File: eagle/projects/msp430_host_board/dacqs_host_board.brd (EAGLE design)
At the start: 127 x 100 mm, 272 parts, among them J1 MOL-SL-4-RA, J10 MOL-SL-3-V, J11 MOL-SL-2-V, J12 CONN HEADER 20POS .100" DBL, J13 MOL-SL-2-RA, J14 USB_MICROB_RECPT, J16 MOL-SL-2-RA, J17 CLM-112-02-L-D-IMU-MOUNT_IMU, J18 MOLSL-7-RA, J19 CONN HEADER 20POS .100" DBL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

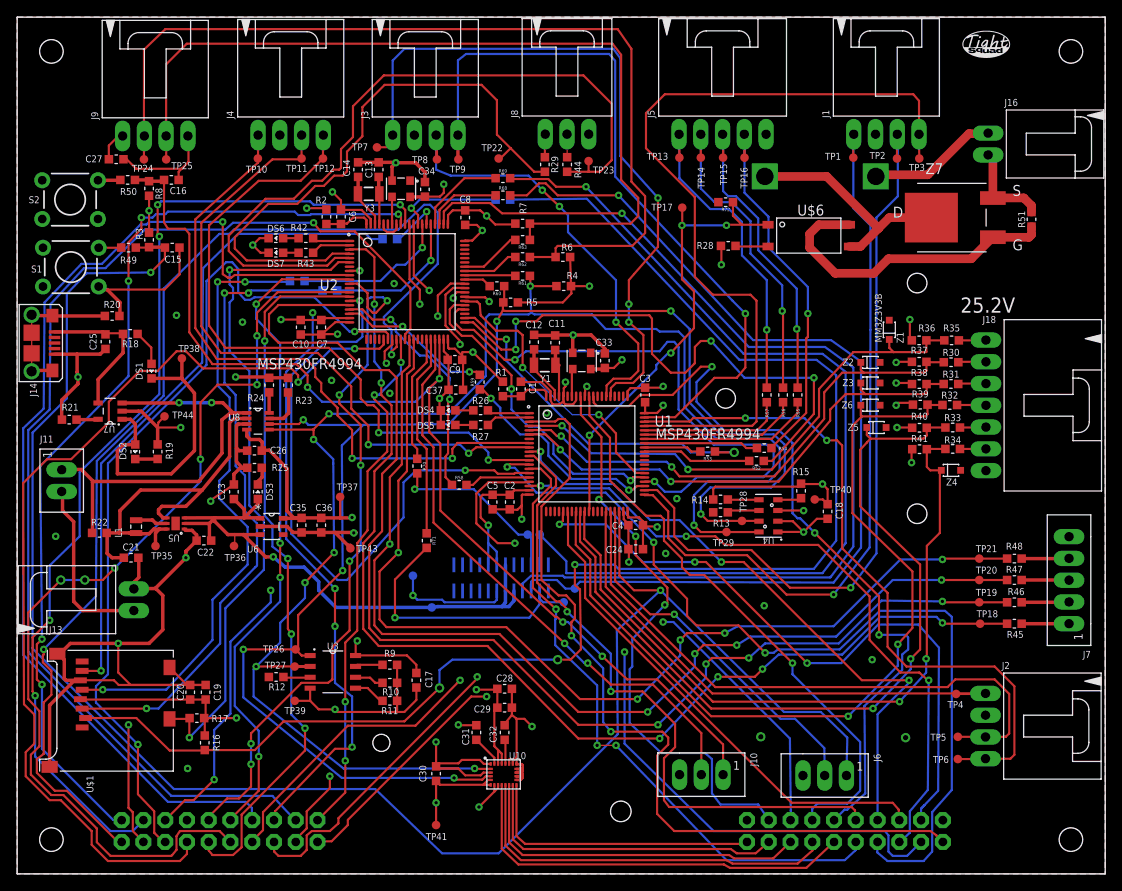
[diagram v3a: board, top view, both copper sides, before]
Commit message: Changed the power fet symbol and attached the powerpad on the 5V boost to ground pour
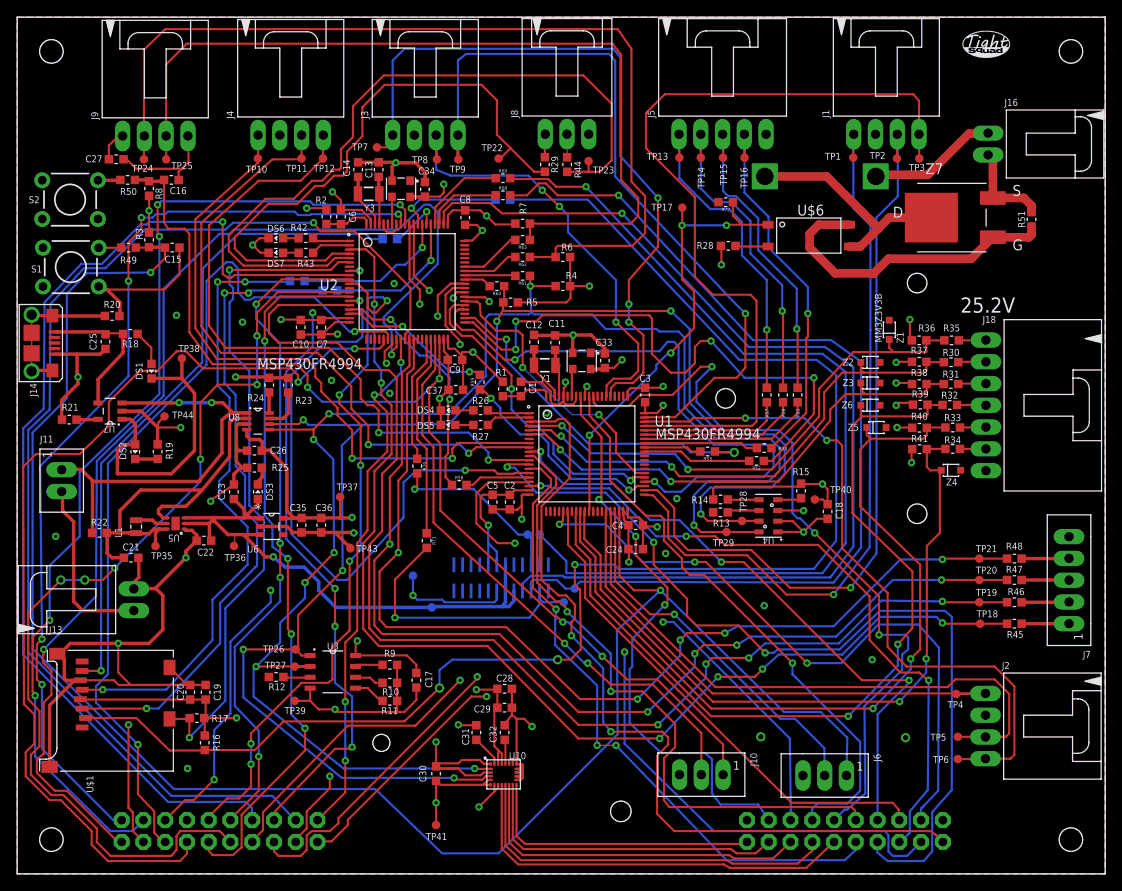
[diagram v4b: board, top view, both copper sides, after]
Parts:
- moved R4 0.10 mm to (63.7, 69.6)
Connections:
- removed net N$42: U5.7
- net GND: now also U5.7
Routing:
- net P7.2_2: track 115.0 -> 116.3 mm
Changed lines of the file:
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@@
 <layer number="14" name="Route14" color="1" fill="6" visible="no" active="no"/>
 <layer number="15" name="Route15" color="4" fill="6" visible="yes" active="yes"/>
-<layer number="16" name="Bottom" color="1" fill="1" visible="no" active="yes"/>
+<layer number="16" name="Bottom" color="1" fill="1" visible="yes" active="yes"/>
 <layer number="17" name="Pads" color="2" fill="1" visible="yes" active="yes"/>
 <layer number="18" name="Vias" color="2" fill="1" visible="yes" active="yes"/>
@@
 <attribute name="VALUE" value="1.02k" x="105.41" y="56.52" size="0.254" layer="27" ratio="6" rot="R180" align="center"/>
 </element>
-<element name="R4" library="daqcs_host" package="R0603" value="2.61k" x="63.8" y="69.6" smashed="yes">
-<attribute name="MANUFACTURER" value="Panasonic" x="63.8" y="69.6" size="1.778" layer="27" display="off"/>
-<attribute name="MANUFACTURER_PN" value="ERJ-3EKF2611V" x="63.8" y="69.6" size="1.778" layer="27" display="off"/>
-<attribute name="VENDOR" value="Digi-key" x="63.8" y="69.6" size="1.778" layer="27" display="off"/>
-<attribute name="POWER" value="1/10W" x="63.8" y="69.6" size="1.778" layer="27" display="off"/>
-<attribute name="VENDOR_PN" value="P2.61KHCT-ND" x="63.8" y="69.6" size="1.778" layer="27" display="off"/>
-<attribute name="TOLERANCE" value="1%" x="63.8" y="69.6" size="1.778" layer="27" display="off"/>
-<attribute name="NAME" x="64.8" y="70.85" size="0.8128" layer="25" ratio="15" align="center"/>
-<attribute name="VALUE" x="63.8" y="68.85" size="0.254" layer="27" ratio="6" align="center"/>
+<element name="R4" library="daqcs_host" package="R0603" value="2.61k" x="63.7" y="69.6" smashed="yes">
+<attribute name="MANUFACTURER" value="Panasonic" x="63.7" y="69.6" size="1.778" layer="27" display="off"/>
+<attribute name="MANUFACTURER_PN" value="ERJ-3EKF2611V" x="63.7" y="69.6" size="1.778" layer="27" display="off"/>
+<attribute name="VENDOR" value="Digi-key" x="63.7" y="69.6" size="1.778" layer="27" display="off"/>
+<attribute name="POWER" value="1/10W" x="63.7" y="69.6" size="1.778" layer="27" display="off"/>
+<attribute name="VENDOR_PN" value="P2.61KHCT-ND" x="63.7" y="69.6" size="1.778" layer="27" display="off"/>
+<attribute name="TOLERANCE" value="1%" x="63.7" y="69.6" size="1.778" layer="27" display="off"/>
+<attribute name="NAME" x="64.7" y="70.85" size="0.8128" layer="25" ratio="15" align="center"/>
+<attribute name="VALUE" x="63.7" y="68.85" size="0.254" layer="27" ratio="6" align="center"/>
 </element>
 <element name="R40" library="daqcs_host" package="R0603" value="4.32k" x="105.32" y="53.07" smashed="yes" rot="R180">
@@
 <wire x1="68.6" y1="60.05" x2="69.65" y2="60.05" width="0.254" layer="1"/>
 <wire x1="69.65" y1="60.05" x2="70.6" y2="61" width="0.254" layer="1"/>
-<wire x1="58.45" y1="67.7" x2="63.7" y2="67.7" width="0.254" layer="1"/>
-<wire x1="63.7" y1="67.7" x2="64.7" y2="68.75" width="0.254" layer="1"/>
-<wire x1="64.7" y1="68.75" x2="64.65" y2="69.6" width="0.254" layer="1"/>
+<wire x1="58.45" y1="67.7" x2="64.1" y2="67.7" width="0.254" layer="1"/>
 <wire x1="55.275" y1="13.835" x2="54.465" y2="13.835" width="0.254" layer="1"/>
 <wire x1="54.465" y1="13.835" x2="54" y2="14.3" width="0.254" layer="1"/>
@@
 <wire x1="49.15" y1="13.3" x2="48.9" y2="13.55" width="0.254" layer="1"/>
 <via x="66.8" y="69.6" extent="1-16" drill="0.381"/>
-<wire x1="66.8" y1="69.6" x2="64.65" y2="69.6" width="0.254" layer="1"/>
+<wire x1="66.8" y1="69.6" x2="64.55" y2="69.6" width="0.254" layer="1"/>
 <wire x1="35.55" y1="63.8" x2="35.5" y2="63.95" width="0.254" layer="1"/>
 <wire x1="37.15" y1="65.4" x2="35.5" y2="63.95" width="0.254" layer="1"/>
@@
 <wire x1="71.6" y1="57.7" x2="73.25" y2="57.7" width="0.254" layer="1"/>
 <wire x1="73.25" y1="57.7" x2="73.3" y2="57.75" width="0.254" layer="1"/>
-<wire x1="64.65" y1="69.6" x2="64.55" y2="73" width="0.254" layer="1"/>
+<wire x1="64.55" y1="69.6" x2="64.55" y2="73" width="0.254" layer="1"/>
 <wire x1="54.8" y1="77.8" x2="55.8" y2="76.8" width="0.254" layer="1"/>
 <wire x1="55.8" y1="76.8" x2="58.05" y2="76.8" width="0.254" layer="1"/>
 <wire x1="58.05" y1="76.8" x2="58.15" y2="76.9" width="0.254" layer="1"/>
+<wire x1="64.1" y1="67.7" x2="64.6" y2="68.2" width="0.254" layer="1"/>
+<wire x1="64.6" y1="68.2" x2="64.6" y2="69.55" width="0.254" layer="1"/>
+<wire x1="64.6" y1="69.55" x2="64.55" y2="69.6" width="0.254" layer="1"/>
 </signal>
 <signal name="COMMS_SS">
@@
 <wire x1="43.83" y1="95.93" x2="45.2" y2="97.3" width="0.254" layer="16"/>
 <wire x1="45.2" y1="97.3" x2="69.6" y2="97.3" width="0.254" layer="16"/>
-<wire x1="69.6" y1="97.3" x2="70.4" y2="96.2" width="0.254" layer="16"/>
-<wire x1="70.4" y1="96.2" x2="70.4" y2="84.8" width="0.254" layer="16"/>
+<wire x1="69.6" y1="97.3" x2="70.4" y2="96.3" width="0.254" layer="16"/>
+<wire x1="70.4" y1="96.3" x2="70.4" y2="84.8" width="0.254" layer="16"/>
 <wire x1="70.4" y1="84.8" x2="74.8" y2="79.9" width="0.254" layer="16"/>
 <via x="74.8" y="79.9" extent="1-16" drill="0.381"/>
@@
 <wire x1="82.2" y1="74.25" x2="82.15" y2="74.3" width="0.254" layer="1"/>
 <contactref element="R72" pad="2"/>
+<contactref element="U5" pad="7"/>
 </signal>
 <signal name="AVCC_HOST">
@@
 <wire x1="60" y1="66.5" x2="59.9" y2="69.6" width="0.254" layer="16"/>
 <via x="59.9" y="69.6" extent="1-16" drill="0.381"/>
-<wire x1="59.9" y1="69.6" x2="62.95" y2="69.6" width="0.254" layer="1"/>
+<wire x1="59.9" y1="69.6" x2="62.85" y2="69.6" width="0.254" layer="1"/>
 <wire x1="74.6" y1="64.6" x2="75" y2="64.3" width="0.254" layer="16"/>
 <wire x1="75" y1="64.3" x2="77.2" y2="64.3" width="0.254" layer="16"/>
@@
 <wire x1="95.6" y1="59.2" x2="93.3" y2="61" width="0.254" layer="16"/>
 <wire x1="93.3" y1="61" x2="84.3" y2="61" width="0.254" layer="16"/>
-<wire x1="66.5" y1="79.8" x2="84.3" y2="61" width="0.254" layer="16"/>
+<wire x1="66.6" y1="79.7" x2="84.3" y2="61" width="0.254" layer="16"/>
 <wire x1="27.75" y1="15.45" x2="31.1" y2="18.8" width="0.254" layer="1"/>
 <wire x1="64.6" y1="26" x2="65.8" y2="27.2" width="0.254" layer="1"/>
@@
 <wire x1="63.1" y1="26" x2="64.6" y2="26" width="0.254" layer="1"/>
 <contactref element="R67" pad="1"/>
-<wire x1="66.5" y1="79.8" x2="57.55" y2="79.7" width="0.254" layer="16"/>
+<wire x1="66.6" y1="79.7" x2="57.55" y2="79.7" width="0.254" layer="16"/>
 </signal>
 <signal name="SD_DETECT">
@@
 <wire x1="14.3" y1="59.7" x2="16.4" y2="59.7" width="0.254" layer="1"/>
 <wire x1="10.7" y1="56.1" x2="14.3" y2="59.7" width="0.254" layer="1"/>
-<wire x1="10.7" y1="53.7" x2="10.7" y2="56.1" width="0.254" layer="1"/>
-<wire x1="6.3" y1="49.4" x2="10.7" y2="53.7" width="0.254" layer="1"/>
-<wire x1="3.5" y1="49.4" x2="6.3" y2="49.4" width="0.254" layer="1"/>
+<wire x1="10.7" y1="53.3" x2="10.7" y2="56.1" width="0.254" layer="1"/>
+<wire x1="7.3" y1="50" x2="10.7" y2="53.3" width="0.254" layer="1"/>
+<wire x1="2.2" y1="50" x2="7.3" y2="50" width="0.254" layer="1"/>
 <wire x1="42.8" y1="63.3" x2="42.77" y2="63.395" width="0.1524" layer="1"/>
 <via x="39.4" y="62.3" extent="1-16" drill="0.381"/>
@@
 <wire x1="2" y1="16.2" x2="2" y2="19.6" width="0.254" layer="1"/>
 <wire x1="2" y1="19.6" x2="0.8" y2="20.8" width="0.254" layer="1"/>
-<wire x1="0.8" y1="20.8" x2="0.7" y2="46.6" width="0.254" layer="1"/>
-<wire x1="0.7" y1="46.6" x2="3.5" y2="49.4" width="0.254" layer="1"/>
+<wire x1="0.8" y1="20.8" x2="0.7" y2="48.5" width="0.254" layer="1"/>
+<wire x1="0.7" y1="48.5" x2="2.2" y2="50" width="0.254" layer="1"/>
 <wire x1="19.82" y1="4.73" x2="19.82" y2="3.32" width="0.254" layer="1"/>
 <wire x1="19.82" y1="3.32" x2="19" y2="2.5" width="0.254" layer="1"/>
@@
 <wire x1="6.6" y1="32.8" x2="6.6" y2="42.1" width="0.4064" layer="1"/>
 </signal>
-<signal name="N$42">
-<contactref element="U5" pad="7"/>
-</signal>
 <signal name="N$43">

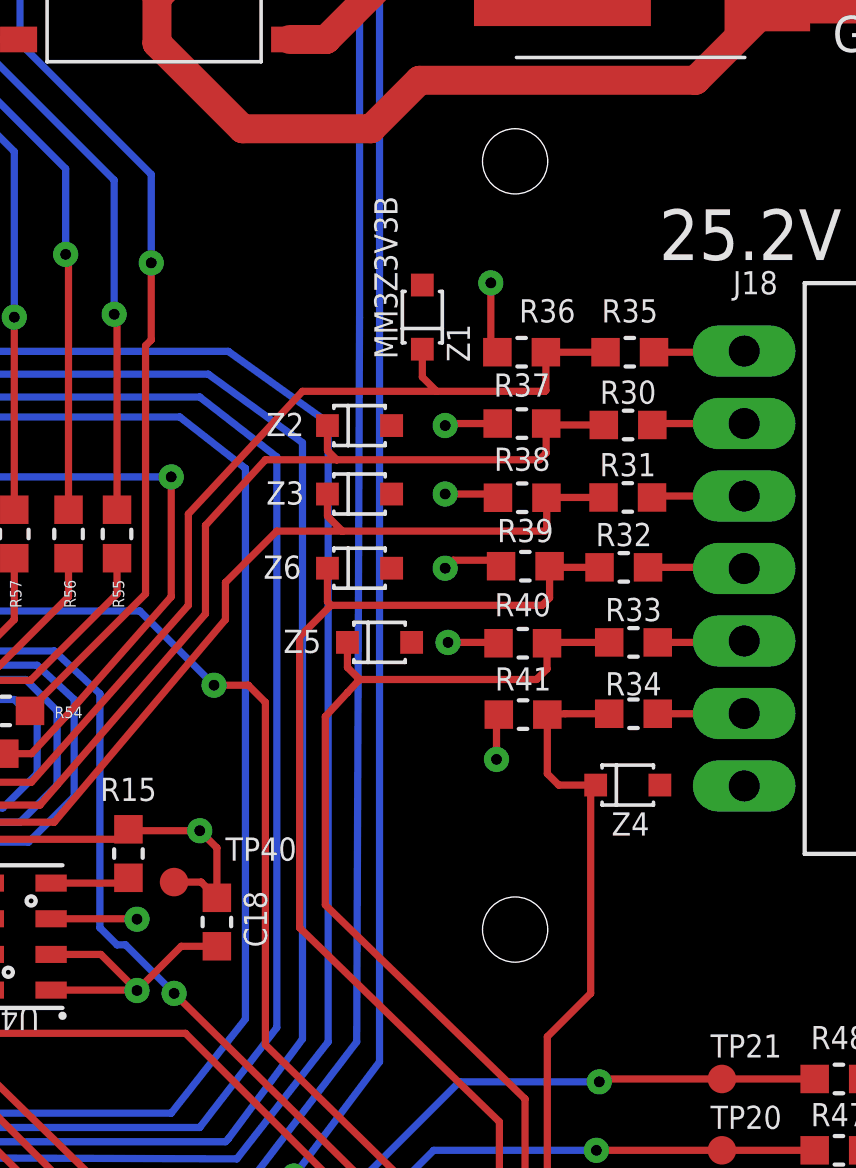
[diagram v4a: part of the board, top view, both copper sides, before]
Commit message: Changed the Zener diodes to 3V Zener voltage
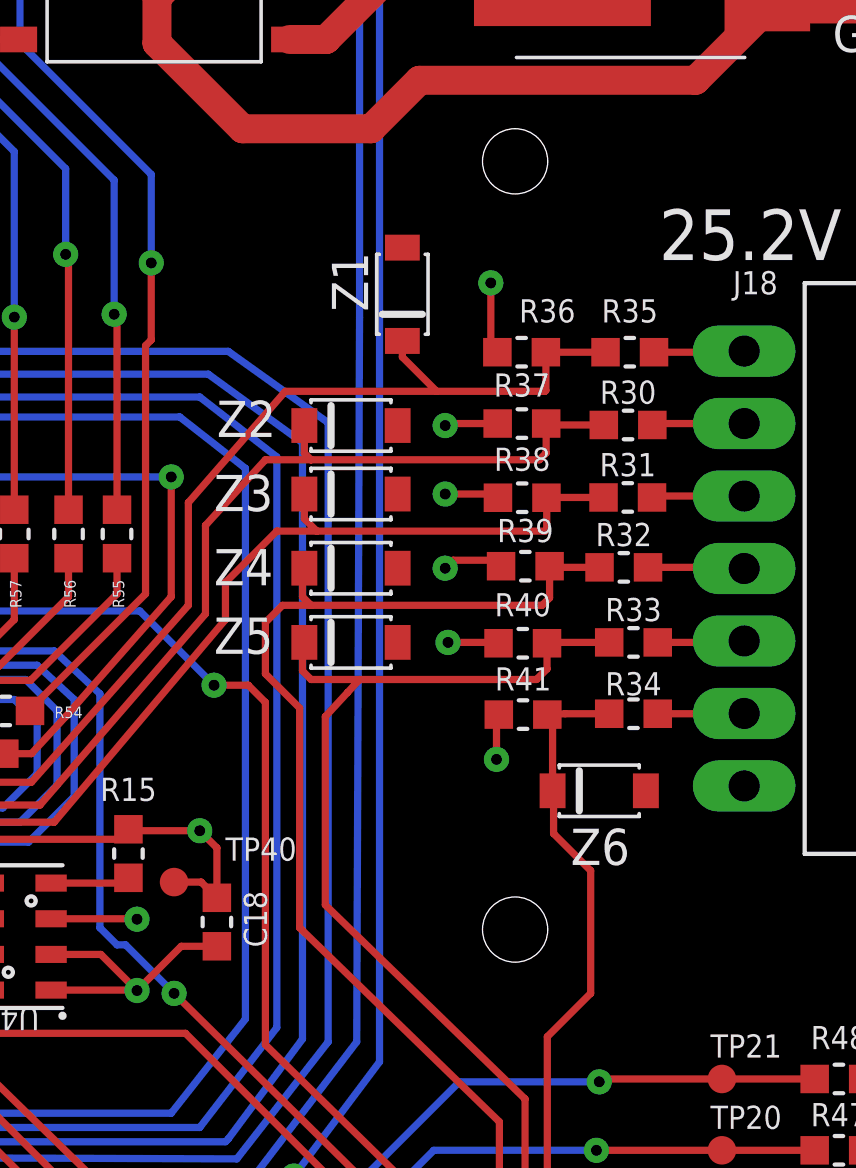
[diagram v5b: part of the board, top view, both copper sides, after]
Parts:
- Z1, Z2, Z3, Z4, Z5, Z6: value MM3Z3V3B -> MMSZ5225BT1G; device daqcs_host:MM3Z3V3B -> daqcs_host:MMSZ5225BT1G
- moved Z4 12.3 mm to (99.3, 55.7)
- moved Z6 11.5 mm to (108.0, 47.9)
- moved Z1 1.06 mm to (101.1, 65.3)
- moved Z5 1.00 mm to (99.3, 53.1)
- moved Z2 0.30 mm to (99.3, 60.7)
- moved Z3 0.30 mm to (99.3, 58.3)
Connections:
- net GND: now also Z1.P$2, Z2.P$2, Z3.P$2, Z4.P$2, Z5.P$2, Z6.P$2; no longer Z1.P$1, Z2.P$1, Z3.P$1, Z4.P$1, Z5.P$1, Z6.P$1
- net VBAT_MOD_CELL_1: now also Z1.P$1; no longer Z1.P$2
- net VBAT_MOD_CELL_2: now also Z2.P$1; no longer Z2.P$2
- net VBAT_MOD_CELL_3: now also Z3.P$1; no longer Z3.P$2
- net VBAT_MOD_CELL_4: now also Z4.P$1; no longer Z6.P$2
- net VBAT_MOD_CELL_5: now also Z5.P$1; no longer Z5.P$2
- net VBAT_MOD_CELL_6: now also Z6.P$1; no longer Z4.P$2
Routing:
- net VBAT_MOD_CELL_4: track 99.9 -> 102.0 mm
- net VBAT_MOD_CELL_5: track 96.7 -> 98.3 mm
- net VBAT_MOD_CELL_6: track 85.3 -> 84.4 mm
- net VBAT_MOD_CELL_1: track 61.5 -> 62.3 mm
